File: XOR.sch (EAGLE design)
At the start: 63 parts, among them IC1 40106D, IC2 4030D, IC3 4520D, IC7 TL074D

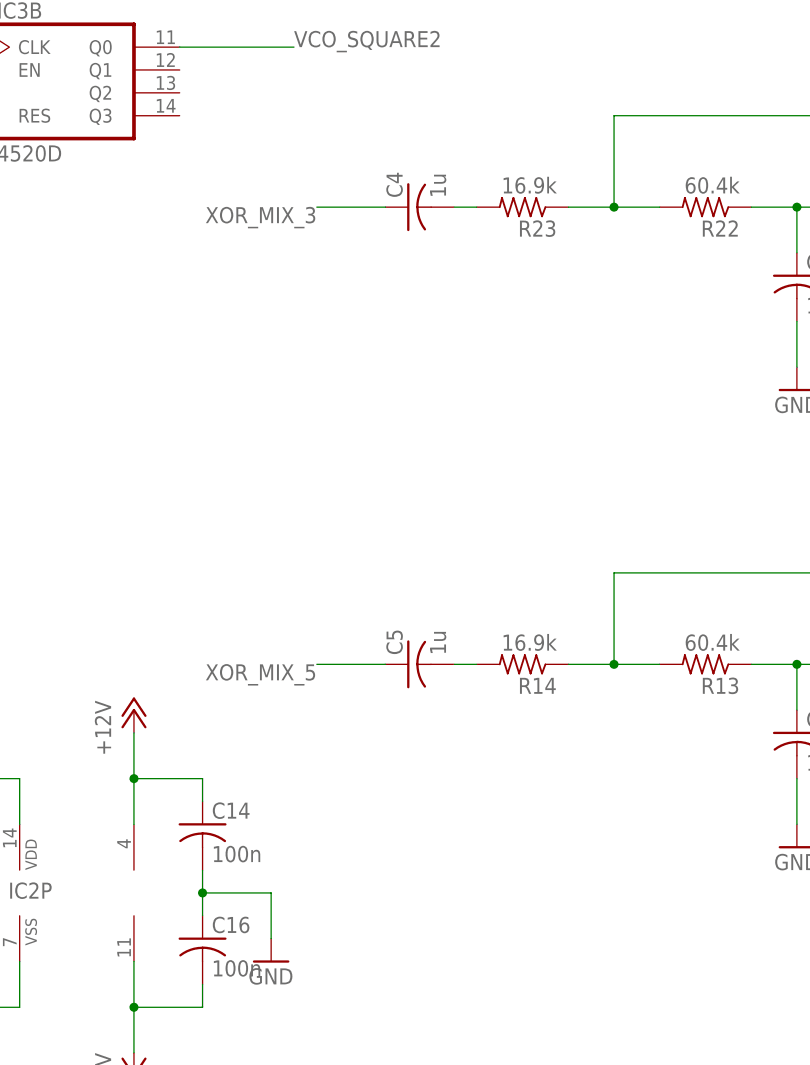
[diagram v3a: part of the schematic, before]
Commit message: Added 2x10k resistors that pulls the filter inputs to ground (got DC offset problem on the filter outputs without them).
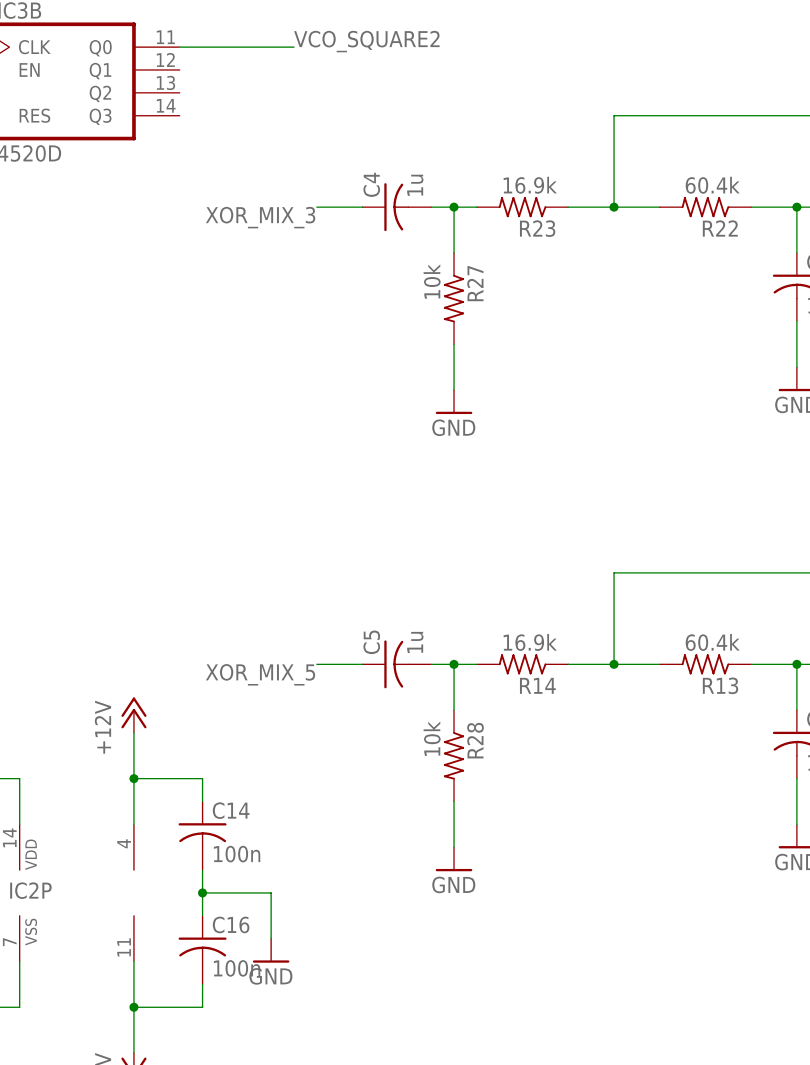
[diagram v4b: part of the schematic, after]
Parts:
- added R27, R28: 10k, rcl:R-US_R0603
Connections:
- net GND: now also R27.2, R28.2
- net N$33: now also R27.1
- net N$38: now also R28.1
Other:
- moved on the sheet: C4, C5
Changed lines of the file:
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@@
 <grid distance="0.1" unitdist="inch" unit="inch" style="lines" multiple="1" display="no" altdistance="0.01" altunitdist="inch" altunit="inch"/>
 <layers>
-<layer number="1" name="Top" color="4" fill="1" visible="yes" active="no"/>
-<layer number="16" name="Bottom" color="1" fill="1" visible="yes" active="no"/>
-<layer number="17" name="Pads" color="2" fill="1" visible="yes" active="no"/>
-<layer number="18" name="Vias" color="2" fill="1" visible="yes" active="no"/>
-<layer number="19" name="Unrouted" color="6" fill="1" visible="yes" active="no"/>
-<layer number="20" name="Dimension" color="15" fill="1" visible="yes" active="no"/>
-<layer number="21" name="tPlace" color="7" fill="1" visible="yes" active="no"/>
-<layer number="22" name="bPlace" color="7" fill="1" visible="yes" active="no"/>
-<layer number="23" name="tOrigins" color="15" fill="1" visible="yes" active="no"/>
-<layer number="24" name="bOrigins" color="15" fill="1" visible="yes" active="no"/>
-<layer number="25" name="tNames" color="7" fill="1" visible="yes" active="no"/>
-<layer number="26" name="bNames" color="7" fill="1" visible="yes" active="no"/>
-<layer number="27" name="tValues" color="7" fill="1" visible="yes" active="no"/>
-<layer number="28" name="bValues" color="7" fill="1" visible="yes" active="no"/>
+<layer number="1" name="Top" color="4" fill="1" visible="no" active="no"/>
+<layer number="16" name="Bottom" color="1" fill="1" visible="no" active="no"/>
+<layer number="17" name="Pads" color="2" fill="1" visible="no" active="no"/>
+<layer number="18" name="Vias" color="2" fill="1" visible="no" active="no"/>
+<layer number="19" name="Unrouted" color="6" fill="1" visible="no" active="no"/>
+<layer number="20" name="Dimension" color="15" fill="1" visible="no" active="no"/>
+<layer number="21" name="tPlace" color="7" fill="1" visible="no" active="no"/>
+<layer number="22" name="bPlace" color="7" fill="1" visible="no" active="no"/>
+<layer number="23" name="tOrigins" color="15" fill="1" visible="no" active="no"/>
+<layer number="24" name="bOrigins" color="15" fill="1" visible="no" active="no"/>
+<layer number="25" name="tNames" color="7" fill="1" visible="no" active="no"/>
+<layer number="26" name="bNames" color="7" fill="1" visible="no" active="no"/>
+<layer number="27" name="tValues" color="7" fill="1" visible="no" active="no"/>
+<layer number="28" name="bValues" color="7" fill="1" visible="no" active="no"/>
 <layer number="29" name="tStop" color="7" fill="3" visible="no" active="no"/>
 <layer number="30" name="bStop" color="7" fill="6" visible="no" active="no"/>
@@
 <layer number="35" name="tGlue" color="7" fill="4" visible="no" active="no"/>
 <layer number="36" name="bGlue" color="7" fill="5" visible="no" active="no"/>
-<layer number="37" name="tTest" color="7" fill="1" visible="yes" active="no"/>
-<layer number="38" name="bTest" color="7" fill="1" visible="yes" active="no"/>
+<layer number="37" name="tTest" color="7" fill="1" visible="no" active="no"/>
+<layer number="38" name="bTest" color="7" fill="1" visible="no" active="no"/>
 <layer number="39" name="tKeepout" color="4" fill="11" visible="no" active="no"/>
 <layer number="40" name="bKeepout" color="1" fill="11" visible="no" active="no"/>
@@
 <layer number="44" name="Drills" color="7" fill="1" visible="no" active="no"/>
 <layer number="45" name="Holes" color="7" fill="1" visible="no" active="no"/>
-<layer number="46" name="Milling" color="3" fill="1" visible="yes" active="no"/>
-<layer number="47" name="Measures" color="7" fill="1" visible="yes" active="no"/>
-<layer number="48" name="Document" color="7" fill="1" visible="yes" active="no"/>
-<layer number="49" name="Reference" color="7" fill="1" visible="yes" active="no"/>
-<layer number="50" name="dxf" color="7" fill="1" visible="yes" active="no"/>
-<layer number="51" name="tDocu" color="7" fill="1" visible="yes" active="no"/>
-<layer number="52" name="bDocu" color="7" fill="1" visible="yes" active="no"/>
-<layer number="53" name="tGND_GNDA" color="7" fill="1" visible="yes" active="no"/>
-<layer number="54" name="bGND_GNDA" color="7" fill="1" visible="yes" active="no"/>
-<layer number="56" name="wert" color="7" fill="1" visible="yes" active="no"/>
-<layer number="57" name="tCAD" color="7" fill="1" visible="yes" active="no"/>
+<layer number="46" name="Milling" color="3" fill="1" visible="no" active="no"/>
+<layer number="47" name="Measures" color="7" fill="1" visible="no" active="no"/>
+<layer number="48" name="Document" color="7" fill="1" visible="no" active="no"/>
+<layer number="49" name="Reference" color="7" fill="1" visible="no" active="no"/>
+<layer number="50" name="dxf" color="7" fill="1" visible="no" active="no"/>
+<layer number="51" name="tDocu" color="7" fill="1" visible="no" active="no"/>
+<layer number="52" name="bDocu" color="7" fill="1" visible="no" active="no"/>
+<layer number="53" name="tGND_GNDA" color="7" fill="1" visible="no" active="no"/>
+<layer number="54" name="bGND_GNDA" color="7" fill="1" visible="no" active="no"/>
+<layer number="56" name="wert" color="7" fill="1" visible="no" active="no"/>
+<layer number="57" name="tCAD" color="7" fill="1" visible="no" active="no"/>
 <layer number="90" name="Modules" color="5" fill="1" visible="yes" active="yes"/>
 <layer number="91" name="Nets" color="2" fill="1" visible="yes" active="yes"/>
@@
 <part name="C15" library="rcl" deviceset="C-US" device="C0603K" value="100n"/>
 <part name="C22" library="rcl" deviceset="C-US" device="C0603K" value="100n"/>
+<part name="R27" library="rcl" deviceset="R-US_" device="R0603" value="10k"/>
+<part name="R28" library="rcl" deviceset="R-US_" device="R0603" value="10k"/>
+<part name="GND24" library="supply1" deviceset="GND" device=""/>
+<part name="GND25" library="supply1" deviceset="GND" device=""/>
 </parts>
 <sheets>
@@
 <instance part="GND19" gate="1" x="55.88" y="104.14"/>
 <instance part="GND20" gate="1" x="55.88" y="175.26"/>
-<instance part="C4" gate="G$1" x="175.26" y="116.84" rot="R90"/>
-<instance part="C5" gate="G$1" x="175.26" y="66.04" rot="R90"/>
+<instance part="C4" gate="G$1" x="172.72" y="116.84" rot="R90"/>
+<instance part="C5" gate="G$1" x="172.72" y="66.04" rot="R90"/>
 <instance part="P-3" gate="1" x="121.92" y="190.5"/>
 <instance part="P-4" gate="1" x="121.92" y="119.38"/>
@@
 <instance part="C15" gate="G$1" x="91.44" y="43.18"/>
 <instance part="C22" gate="G$1" x="83.82" y="43.18"/>
+<instance part="R27" gate="G$1" x="180.34" y="106.68" rot="R270"/>
+<instance part="R28" gate="G$1" x="180.34" y="55.88" rot="R270"/>
+<instance part="GND24" gate="1" x="180.34" y="93.98"/>
+<instance part="GND25" gate="1" x="180.34" y="43.18"/>
 </instances>
 <busses>
@@
 <pinref part="GND23" gate="1" pin="GND"/>
 </segment>
+<segment>
+<pinref part="GND24" gate="1" pin="GND"/>
+<pinref part="R27" gate="G$1" pin="2"/>
+<wire x1="180.34" y1="96.52" x2="180.34" y2="101.6" width="0.1524" layer="91"/>
+</segment>
+<segment>
+<pinref part="GND25" gate="1" pin="GND"/>
+<pinref part="R28" gate="G$1" pin="2"/>
+<wire x1="180.34" y1="45.72" x2="180.34" y2="50.8" width="0.1524" layer="91"/>
+</segment>
 </net>
 <net name="N$1" class="0">
@@
 <segment>
 <pinref part="C4" gate="G$1" pin="1"/>
-<wire x1="172.72" y1="116.84" x2="165.1" y2="116.84" width="0.1524" layer="91"/>
+<wire x1="170.18" y1="116.84" x2="165.1" y2="116.84" width="0.1524" layer="91"/>
 <label x="165.1" y="116.84" size="1.778" layer="95" rot="R180"/>
 </segment>
@@
 <segment>
 <pinref part="C5" gate="G$1" pin="1"/>
-<wire x1="172.72" y1="66.04" x2="165.1" y2="66.04" width="0.1524" layer="91"/>
+<wire x1="170.18" y1="66.04" x2="165.1" y2="66.04" width="0.1524" layer="91"/>
 <label x="165.1" y="66.04" size="1.778" layer="95" rot="R180"/>
 </segment>
@@
 <pinref part="C4" gate="G$1" pin="2"/>
 <pinref part="R23" gate="G$1" pin="2"/>
+<wire x1="177.8" y1="116.84" x2="180.34" y2="116.84" width="0.1524" layer="91"/>
+<pinref part="R27" gate="G$1" pin="1"/>
 <wire x1="180.34" y1="116.84" x2="182.88" y2="116.84" width="0.1524" layer="91"/>
+<wire x1="180.34" y1="111.76" x2="180.34" y2="116.84" width="0.1524" layer="91"/>
+<junction x="180.34" y="116.84"/>
 </segment>
 </net>
@@
 <pinref part="C5" gate="G$1" pin="2"/>
 <wire x1="182.88" y1="66.04" x2="180.34" y2="66.04" width="0.1524" layer="91"/>
-</segment>
-</net>
+<pinref part="R28" gate="G$1" pin="1"/>
+<wire x1="180.34" y1="66.04" x2="177.8" y2="66.04" width="0.1524" layer="91"/>
+<wire x1="180.34" y1="60.96" x2="180.34" y2="66.04" width="0.1524" layer="91"/>
+<junction x="180.34" y="66.04"/>
+</segment>
+</net>
